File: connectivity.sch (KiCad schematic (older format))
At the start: 25 parts

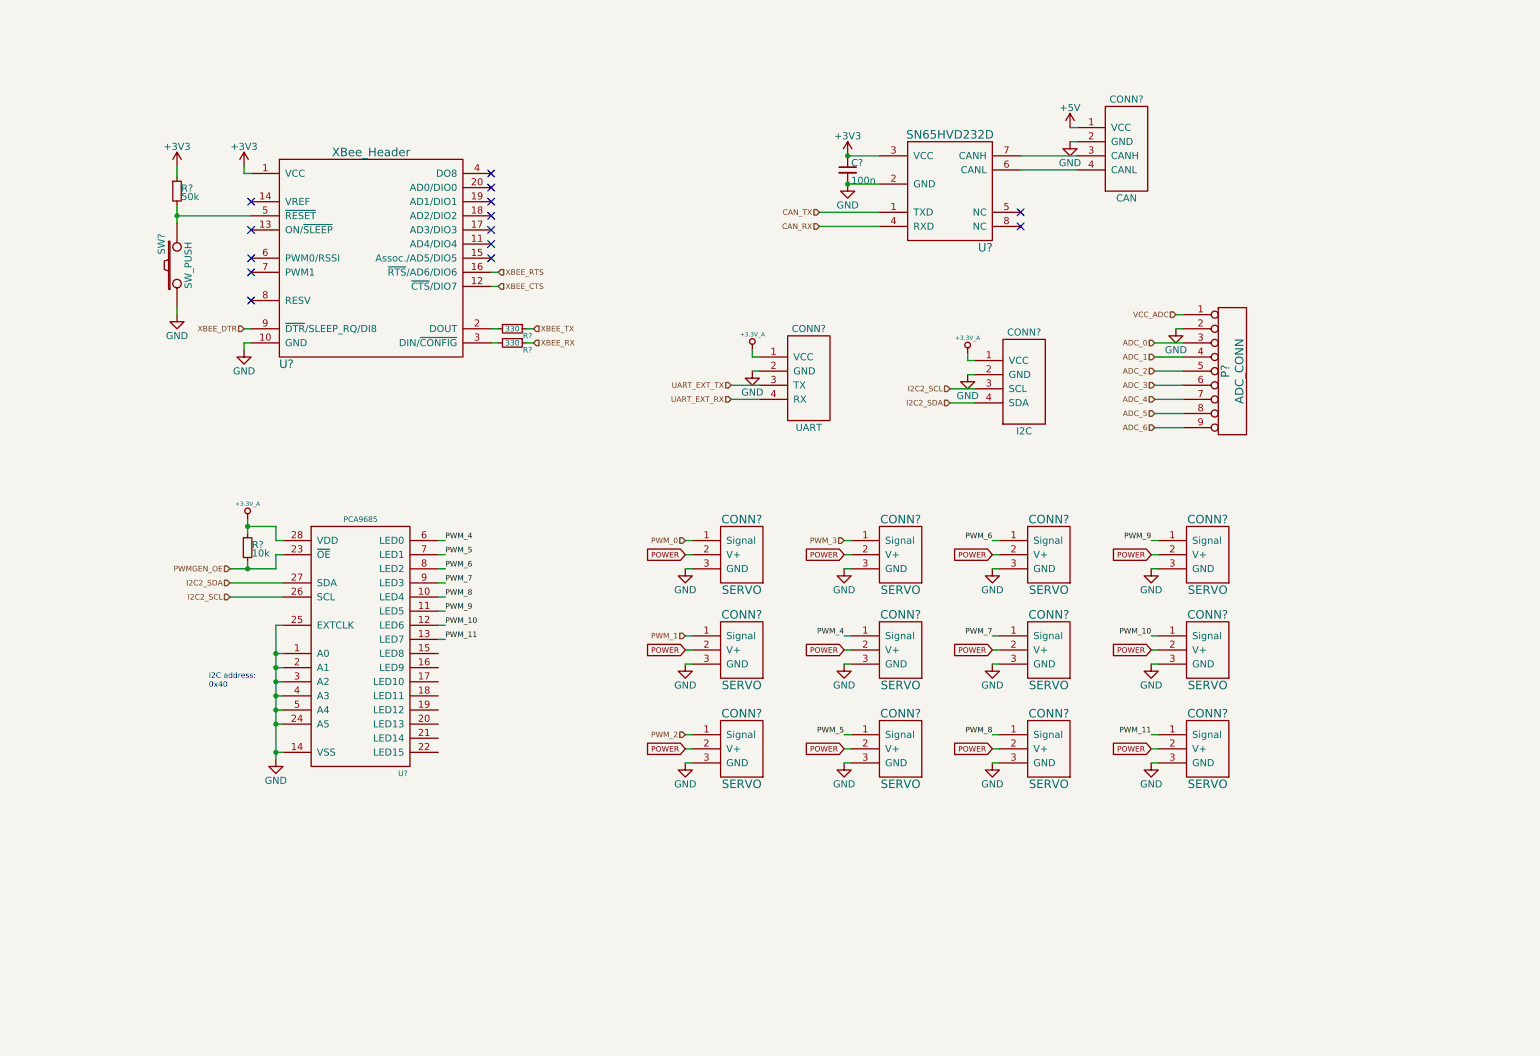
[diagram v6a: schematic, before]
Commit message: Schematics: Minor cleanups
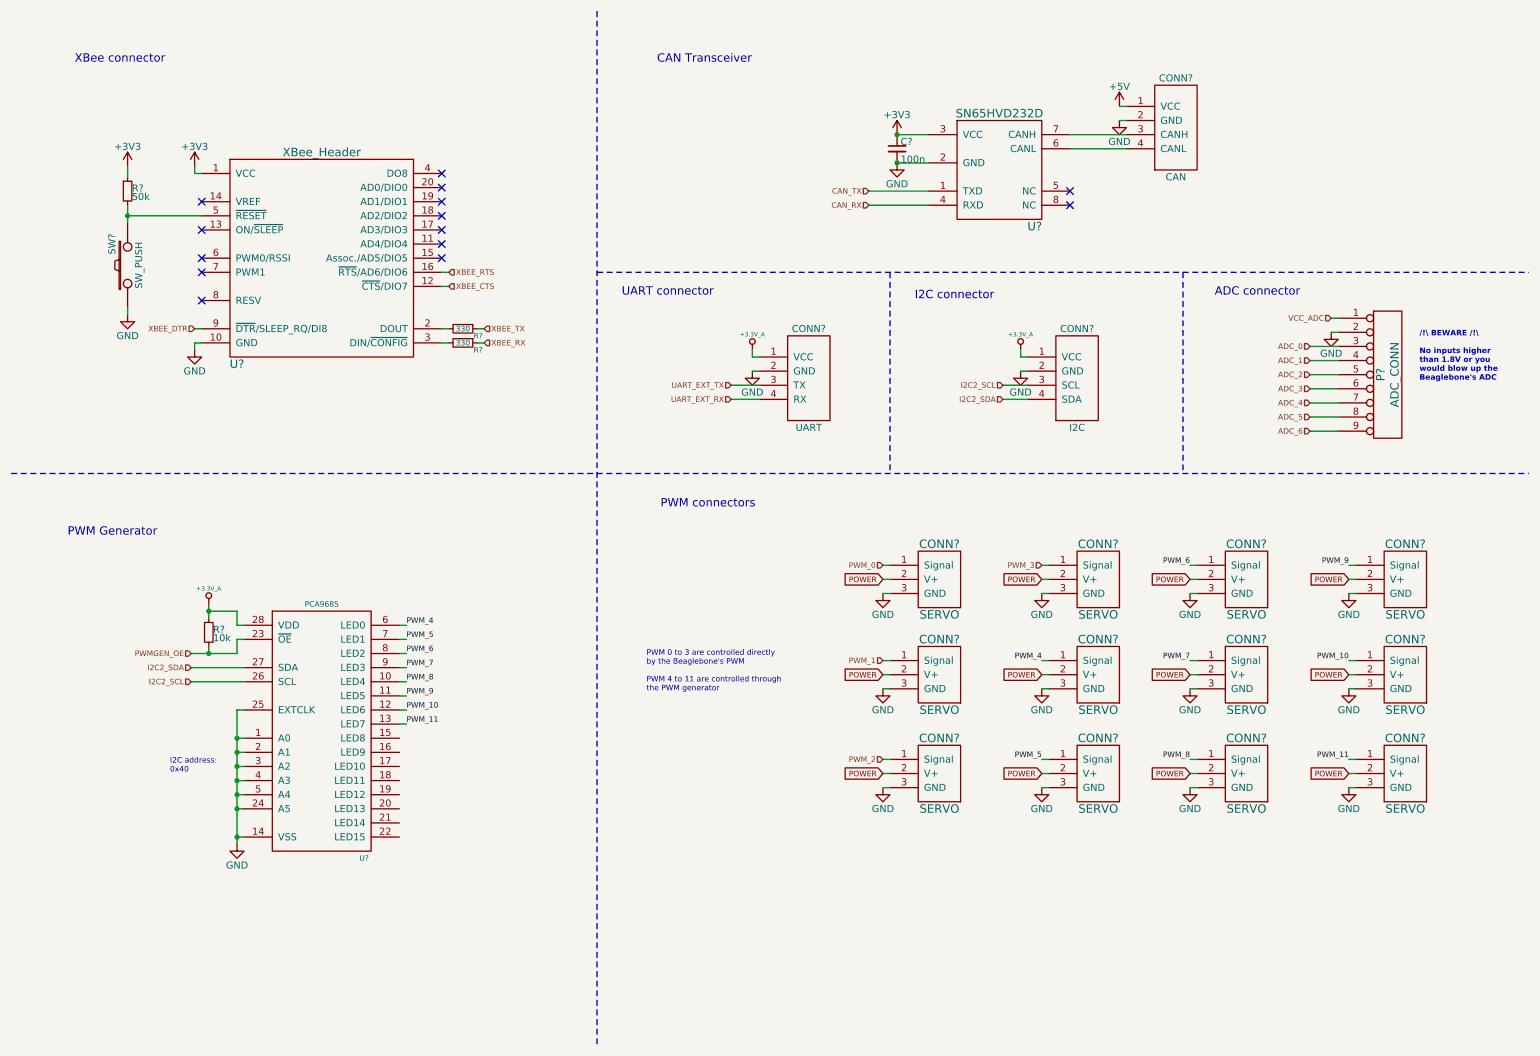
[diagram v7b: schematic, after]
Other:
- note added: "/!\ BEWARE /!\\n\nNo inputs higher \nthan 1.8V or you \nwould blow up the \nBeaglebone's ADC"
- note added: "ADC connector"
- note added: "CAN Transceiver"
- note added: "I2C connector"
- note added: "PWM 0 to 3 are controlled directly \nby the Beaglebone's PWM\n\nPWM 4 to 11 are controlled through \nthe PWM generator"
- note added: "PWM Generator"
- note added: "PWM connectors"
- note added: "UART connector"
- note added: "XBee connector"
- moved on the sheet: C?, CONN?, P?, R?, SW?, U?

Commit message: Schematics: LEDs
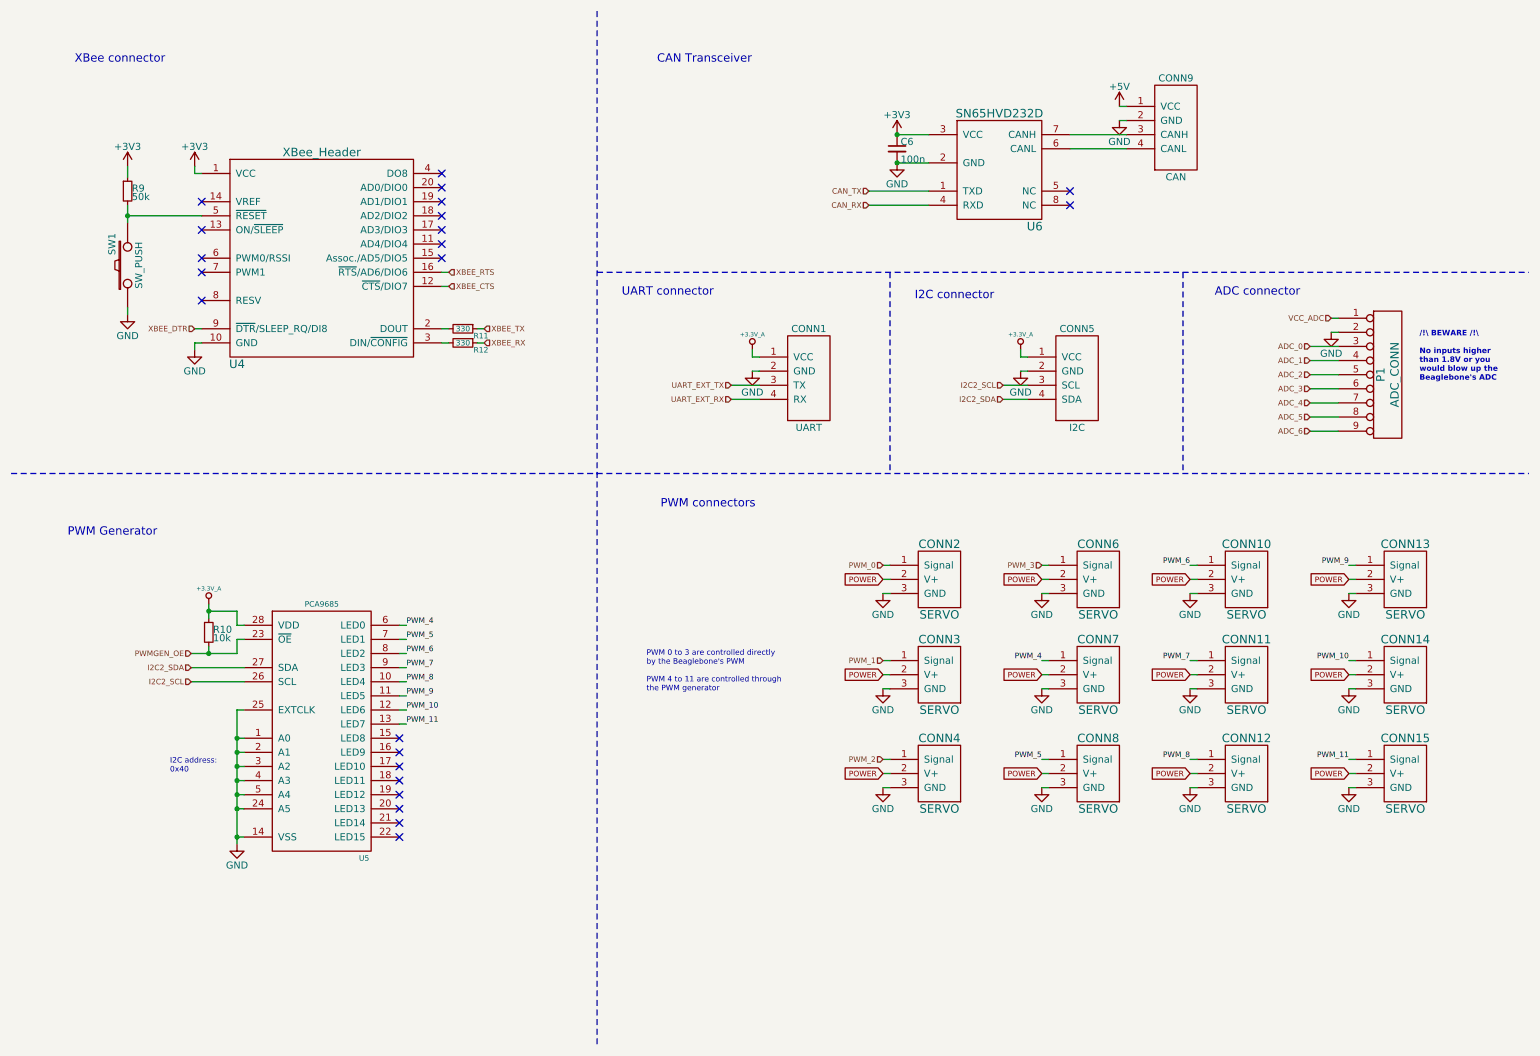
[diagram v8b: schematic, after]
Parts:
- gave numbers to parts that had none: 25
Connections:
- no-connect marks 14 -> 22
